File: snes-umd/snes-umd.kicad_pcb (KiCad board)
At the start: 2 copper layers, 20.3 x 96 mm, 3 parts

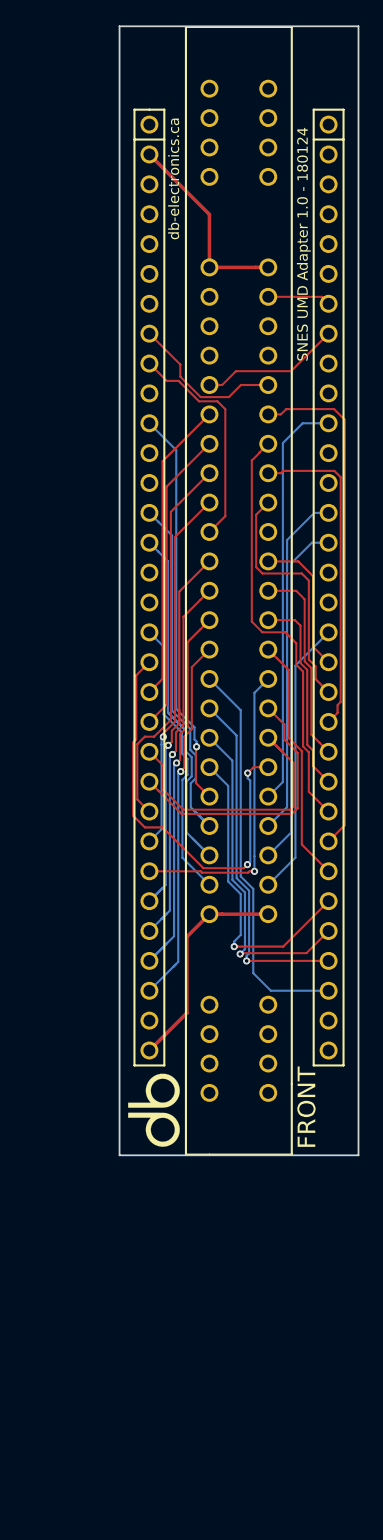
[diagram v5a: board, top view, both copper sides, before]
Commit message: PCB routing verification finished, adjusted date code
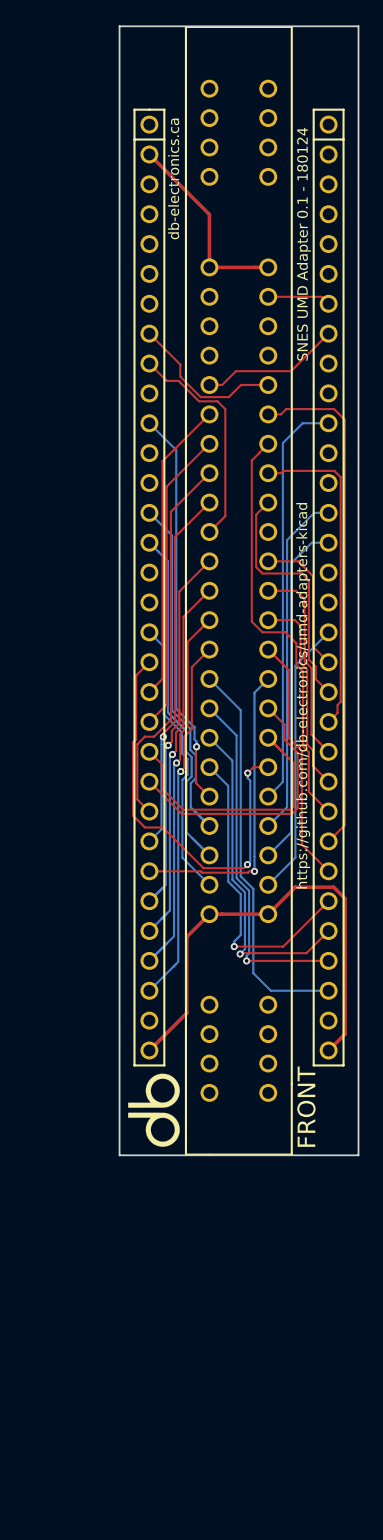
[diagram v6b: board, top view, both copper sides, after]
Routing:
- net GND: track 18.7 -> 40.1 mm
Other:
- net class Default: clearance 0.1778 -> 0.1524
- rule trace_clearance: 0.1778 -> 0.1524
- board text added: "SNES UMD Adapter 0.1 - 180124"
- board text added: "https://github.com/db-electronics/umd-adapters-kicad"
- board text removed: "SNES UMD Adapter 1.0 - 180124"
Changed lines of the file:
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@@
   (general
     (links 41)
-    (no_connects 5)
+    (no_connects 0)
     (area 130.480999 57.825179 150.951001 159.21978)
     (thickness 1.6)
-    (drawings 11)
-    (tracks 296)
+    (drawings 12)
+    (tracks 301)
     (zones 0)
     (modules 3)
     (nets 39)
   )
-  (page A4)
+  (page USLetter)
   (title_block
     (title "SNES UMD Adapter")
-    (date 2018-01-19)
+    (date 2018-01-24)
     (rev 0.1)
     (company "db Electronics")
@@
   (setup
     (last_trace_width 0.1778)
-    (trace_clearance 0.1778)
+    (trace_clearance 0.1524)
     (zone_clearance 0.508)
     (zone_45_only no)
@@
     (visible_elements FFFFFF7F)
     (pcbplotparams
-      (layerselection 0x00030_80000001)
-      (usegerberextensions false)
+      (layerselection 0x010f0_80000001)
+      (usegerberextensions true)
       (excludeedgelayer true)
       (linewidth 0.100000)
@@
       (psa4output false)
       (plotreference true)
-      (plotvalue true)
+      (plotvalue false)
       (plotinvisibletext false)
       (padsonsilk false)
@@
       (outputformat 1)
       (mirror false)
-      (drillshape 1)
+      (drillshape 0)
       (scaleselection 1)
-      (outputdirectory ""))
+      (outputdirectory gerbers/))
   )
   (net 0 "")
@@
   (net 38 /~CE)
   (net_class Default "This is the default net class."
-    (clearance 0.1778)
+    (clearance 0.1524)
     (trace_width 0.1778)
     (via_dia 0.6096)
@@
       (xy 0.220206 -0.700617) (xy 0.220133 -2.184401) (xy 0.643466 -2.184401) (xy 0.643466 -0.262528)) (layer F.SilkS) (width 0.01))
   )
+  (gr_text https://github.com/db-electronics/umd-adapters-kicad (at 146.09874 114.96328 90) (layer F.SilkS)
+    (effects (font (size 0.889 0.889) (thickness 0.2032)))
+  )
   (gr_text db-electronics.ca (at 135.20214 70.99588 90) (layer F.SilkS)
     (effects (font (size 0.889 0.889) (thickness 0.2032)))
   )
-  (gr_text "SNES UMD Adapter 1.0 - 180124" (at 146.14954 76.58388 90) (layer F.SilkS)
+  (gr_text "SNES UMD Adapter 0.1 - 180124" (at 146.14954 76.58388 90) (layer F.SilkS)
     (effects (font (size 0.889 0.889) (thickness 0.22225)))
   )
@@
   (gr_line (start 130.556 154.051) (end 150.876 154.051) (layer Edge.Cuts) (width 0.15))
   (gr_line (start 130.556 58.039) (end 130.556 154.051) (layer Edge.Cuts) (width 0.15))
+  (segment (start 143.20394 133.54188) (end 145.50114 131.24468) (width 0.3048) (layer F.Cu) (net 1))
+  (segment (start 145.50114 131.24468) (end 148.761538 131.24468) (width 0.3048) (layer F.Cu) (net 1))
+  (segment (start 148.761538 131.24468) (end 149.73094 132.214082) (width 0.3048) (layer F.Cu) (net 1))
+  (segment (start 149.73094 132.214082) (end 149.73094 143.74066) (width 0.3048) (layer F.Cu) (net 1))
+  (segment (start 149.73094 143.74066) (end 148.336 145.1356) (width 0.3048) (layer F.Cu) (net 1))
   (segment (start 138.20394 133.54188) (end 139.28157 133.54188) (width 0.3048) (layer F.Cu) (net 1))
   (segment (start 139.28157 133.54188) (end 143.20394 133.54188) (width 0.3048) (layer F.Cu) (net 1))

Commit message: fixed the backwards nintendo pin numbering scheme
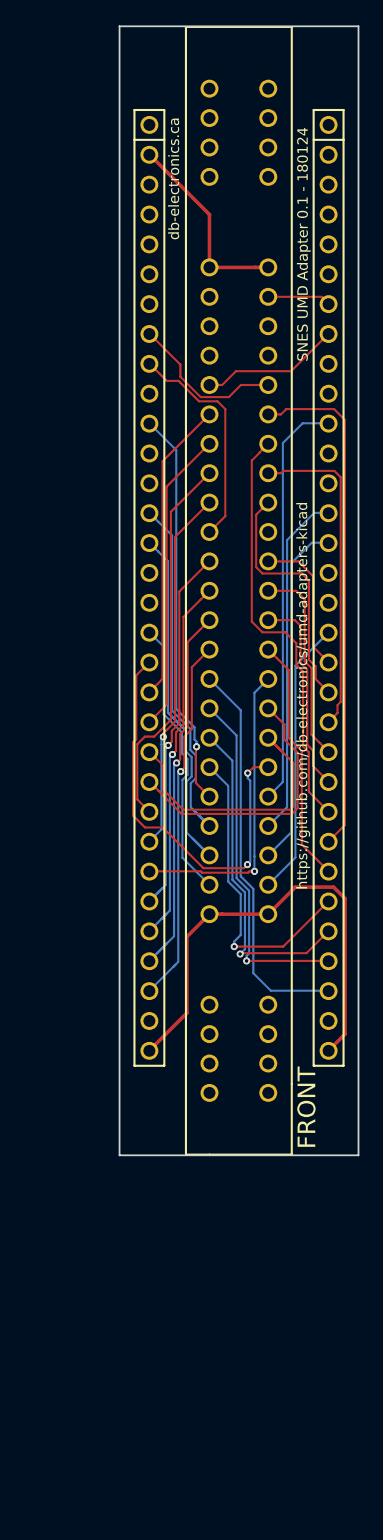
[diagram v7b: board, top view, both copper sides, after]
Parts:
- removed C101: umd-conn, db-thparts:UMD-CONN-DIP64
- removed G***: LOGO, db-artwork:db-logo
- added CON101: UMD-CONN, db-thparts:UMD-CONN-DIP64, F.Cu at (133.1, 66.4)

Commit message: fixed the ass-backwards SNES pin numbering
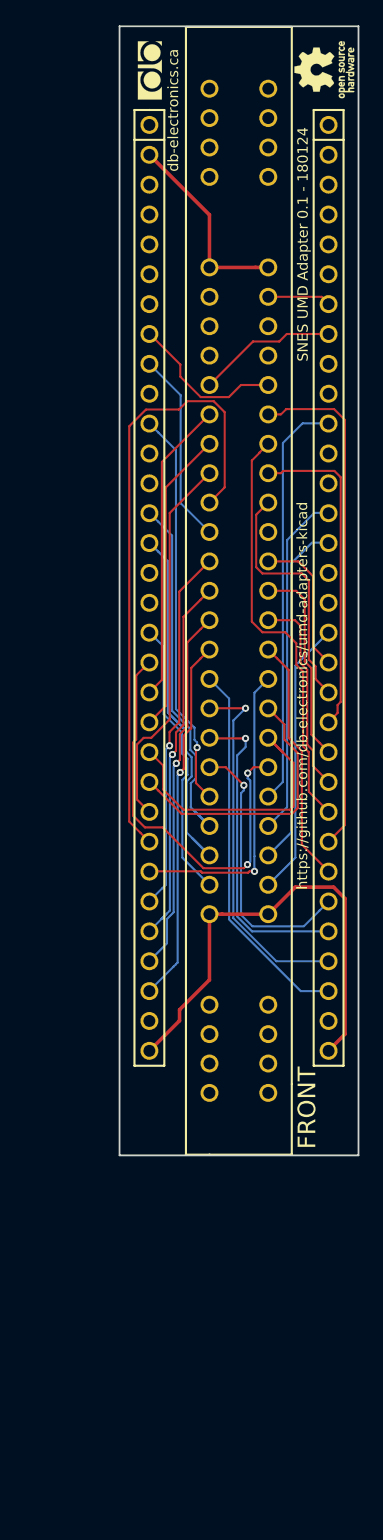
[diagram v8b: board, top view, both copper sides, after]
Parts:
- added G***: LOGO, db-artwork:oshw-logo_5mm, F.Cu at (148.0, 61.7)
- added G***: LOGO, db-artwork:db-logo_5mm, F.Cu at (133.1, 61.8)
- renumbered C102 to CON102
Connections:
- CON102 pad 36: +5V -> GND
- CON102 pad 37: (no net) -> /A12
- CON102 pad 38: (no net) -> /A13
- CON102 pad 39: (no net) -> /A14
- CON102 pad 40: /~WR -> /A15
- CON102 pad 41: /D7 -> /A16
- CON102 pad 42: /D6 -> /A17
- CON102 pad 43: /D5 -> /A18
- CON102 pad 44: /D4 -> /A19
- CON102 pad 45: /~CE -> /A20
- CON102 pad 46: /A23 -> /A21
- CON102 pad 48: /A21 -> /A23
- CON102 pad 49: /A20 -> /~CE
- CON102 pad 50: /A19 -> /D4
- CON102 pad 51: /A18 -> /D5
- CON102 pad 52: /A17 -> /D6
- CON102 pad 53: /A16 -> /D7
- CON102 pad 54: /A15 -> /~WR
- CON102 pad 55: /A14 -> (no net)
- CON102 pad 56: /A13 -> (no net)
- CON102 pad 57: /A12 -> (no net)
- CON102 pad 58: GND -> +5V
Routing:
- net /D4: track 30.9 -> 53.7 mm, vias 1 -> 0
- net /A16: track 26.2 -> 23.4 mm
- net /~CE: track 19.1 -> 16.4 mm
- net /A23: track 33.6 -> 31.0 mm
- net /A21: track 33.2 -> 31.1 mm
- net /A19: track 33.6 -> 32.1 mm
- net /A17: track 28.1 -> 26.8 mm
- net /A18: track 29.9 -> 31.0 mm
